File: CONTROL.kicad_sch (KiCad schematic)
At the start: 24 parts, among them J5 Conn_01x12-Socket, J6 Conn_01x12-Socket, J7 Conn_01x12-Header, J8 Conn_01x12-Header, M1 Fan_4pin, M2 Fan_4pin, U17 TMP1075, U30 T-Display-S3, U32 EMC2302-1, U33 TXU0102-DCU, U37 TMP1075, U38 TMP1075

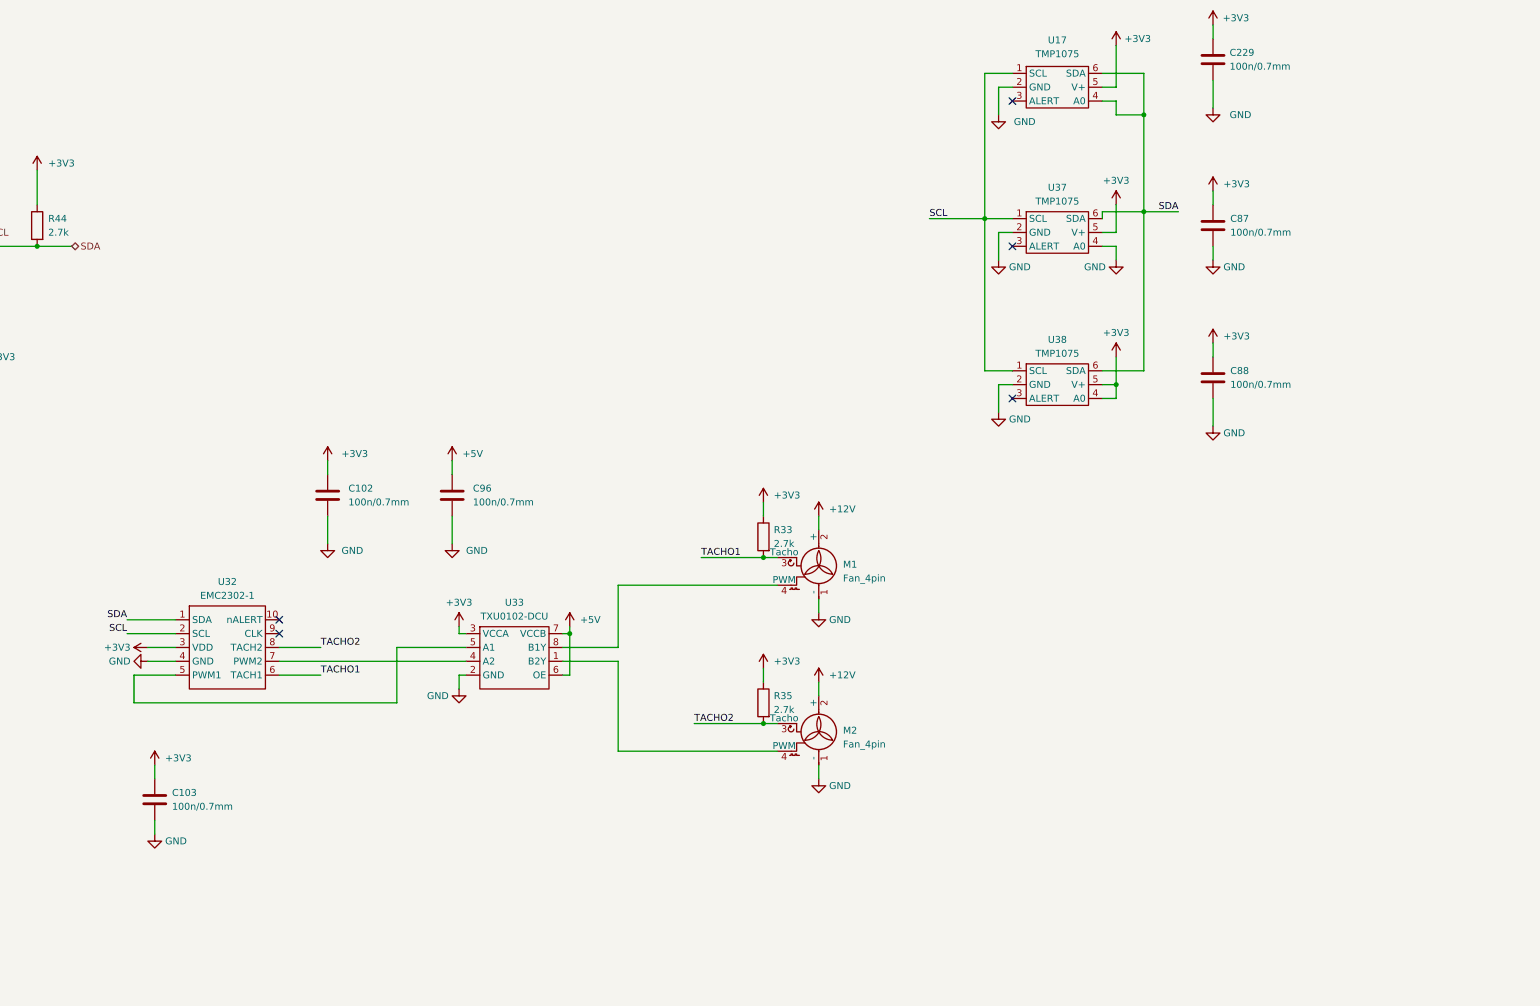
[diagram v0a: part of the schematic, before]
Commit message: shrinking layout to fit
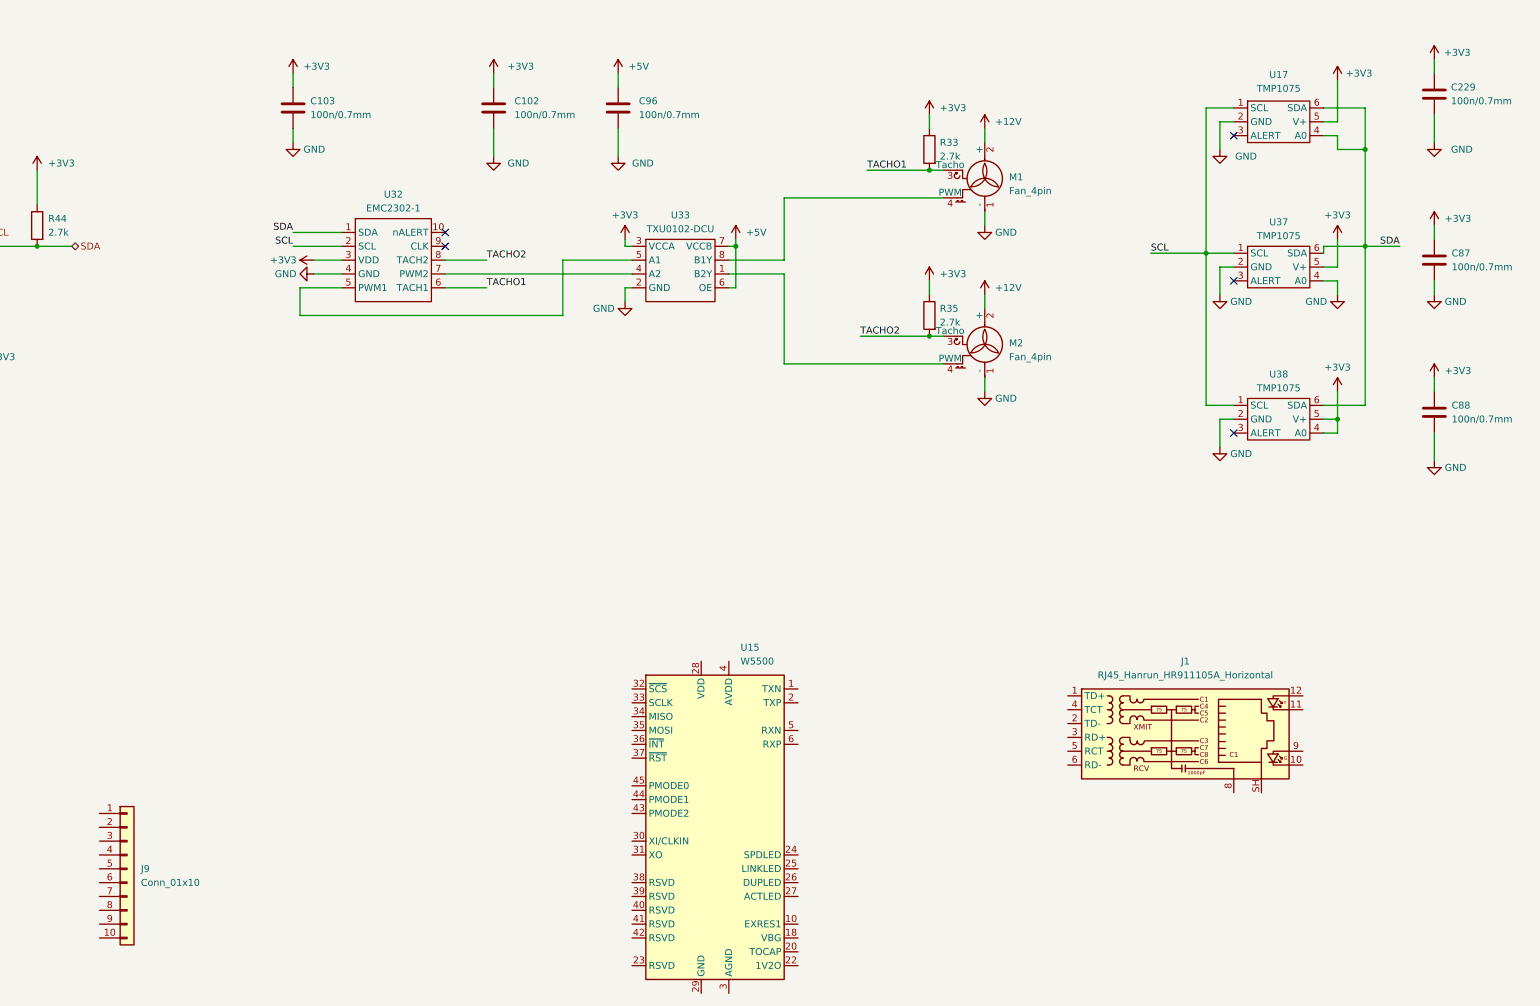
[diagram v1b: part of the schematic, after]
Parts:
- added J1: RJ45_Hanrun_HR911105A_Horizontal, Connector_RJ:RJ45_Hanrun_HR911105A_Horizontal, symbol Connector:RJ45_Hanrun_HR911105A_Horizontal
- added J9: Conn_01x10, Connector_PinHeader_2.54mm:PinHeader_1x10_P2.54mm_Vertical, symbol Connector_Generic:Conn_01x10
- added U15: W5500, Package_QFP:LQFP-48_7x7mm_P0.5mm, symbol Interface_Ethernet:W5500
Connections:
- new net: U15.11 (AVDD), U15.15 (AVDD), U15.17 (AVDD), U15.21 (AVDD), U15.4 (AVDD), U15.8 (AVDD)
- new net: U15.14 (AGND), U15.16 (AGND), U15.19 (AGND), U15.3 (AGND), U15.48 (AGND), U15.9 (AGND)
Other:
- moved on the sheet: C102, C103, C229, C87, C88, C96, M1, M2, R33, R35, U17, U32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

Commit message: W5500
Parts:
- removed J1: RJ45_Hanrun_HR911105A_Horizontal, Connector_RJ:RJ45_Hanrun_HR911105A_Horizontal, symbol Connector:RJ45_Hanrun_HR911105A_Horizontal
- removed U15: W5500, Package_QFP:LQFP-48_7x7mm_P0.5mm, symbol Interface_Ethernet:W5500
- added C128: 15pF, Capacitor_SMD:C_0603_1608Metric, symbol Parts:root_0_CAP_NOPOL_Parts.DbLib
- added C129: 15pF, CAP0402, symbol Parts:root_0_CAP_NOPOL_Parts.DbLib
- added C130, C131, C132, C134, C135, C136, C137, C138, C139: 100nF, CAP0402, symbol Parts:root_0_CAP_NOPOL_Parts.DbLib
- added C133: 4.7uF, CAP0603, symbol Parts:root_0_CAP_NOPOL_Parts.DbLib
- added C140, C141: 6.8nF, CAP0603, symbol Parts:root_1_CAP_NOPOL_Parts.DbLib
- added C142: 22n, CAP0603, symbol Parts:root_0_CAP_NOPOL_Parts.DbLib
- added C143: 1n, CAP1206, symbol Parts:root_1_CAP_NOPOL_Parts.DbLib
- added CON7: HR915340A, HR915340A, symbol Parts:root_0_HR915340A_Parts.DbLib
- added R112, R113, R114: 0R, RES0402, symbol Parts:root_2_Resistor_Parts.DbLib
- added R129, R52, R53: 4k7, RES0402, symbol Parts:root_1_Resistor_Parts.DbLib
- added R153: 33R, RES0402, symbol Parts:root_0_Resistor_Parts.DbLib
- added R41: 1M, Resistor_SMD:R_0603_1608Metric, symbol Parts:root_0_Resistor_Parts.DbLib
- added R42, R45, R46, R49: 3R3, RES0402, symbol Parts:root_0_Resistor_Parts.DbLib
- added R50, R54, R55, R56: 49R9, RES0402, symbol Parts:root_1_Resistor_Parts.DbLib
- added R51: 12k4, RES0402, symbol Parts:root_1_Resistor_Parts.DbLib
- added R57: 10R, RES0603, symbol Parts:root_1_Resistor_Parts.DbLib
- added R58, R59: 330R, RES0402, symbol Parts:root_1_Resistor_Parts.DbLib
- added R60: 1M, RES0603, symbol Parts:root_0_Resistor_Parts.DbLib
- added U12: W5500, QFP50P900X900X160-48N, symbol Parts:root_0_W5500_Parts.DbLib
- added X1: TXM25M0004322JBDDO00T, Crystal:Crystal_SMD_3225-4Pin_3.2x2.5mm, symbol Parts:root_3_XTAL_4_PINS_Parts.DbLib
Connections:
- net GND: now also C128.2, C129.2, C130.2, C131.2, C132.2, C133.2, C134.2, C135.2, C136.2, C137.2, C138.2, C139.2, C142.2, C143.1, R51.1, R60.1, U12.14 (AGND), U12.16 (AGND), U12.19 (AGND), U12.29 (GND), U12.3 (AGND), U12.48 (AGND), U12.9 (AGND), X1.2 (CASE), X1.4 (CASE)
- new net: R112.1, U12.45 (PMODE0)
- new net: R51.2, U12.10 (EXRES1)
- new net: CON7.11 (A), R59.1
- new net: C131.1, U12.22 (1V2O)
- new net: C139.1, CON7.5, R50.1, R54.1
- new net: C142.1, CON7.4, R57.1
- new net: CON7.9 (A), R58.1
- new net: R153.2, U12.34 (MISO)
- new net: C133.1, U12.20 (TOCAP)
- new net: R114.1, U12.43 (PMODE2)
- new net: R113.1, U12.44 (PMODE1)
- new net 3V3: R112.2, R113.2, R114.2, R129.2, R52.2, R53.2
- new net 3V3_ETH: C130.1, C132.1, C134.1, C135.1, C136.1, C137.1, C138.1, R55.2, R56.2, R57.2, R58.2, R59.2, U12.11 (AVDD), U12.15 (AVDD), U12.17 (AVDD), U12.21 (AVDD), U12.28 (VDD), U12.4 (AVDD), U12.8 (AVDD)
- new net ACT_LED_N: CON7.10 (C), U12.27 (ACTLED)
- new net ETHR_N: C141.1, R45.2, R50.2
- new net ETHR_P: C140.1, R49.2, R54.2
- new net ETH_RX_N: C141.2, CON7.6 (RD-)
- new net ETH_RX_P: C140.2, CON7.3 (RD+)
- new net ETH_R_N: R45.1, U12.5 (RXN)
- new net ETH_R_P: R49.1, U12.6 (RXP)
- new net ETH_TX_N: CON7.2 (TD-), R42.2, R56.1
- new net ETH_TX_P: CON7.1 (TD+), R46.2, R55.1
- new net ETH_T_N: R42.1, U12.1 (TXN)
- new net ETH_T_P: R46.1, U12.2 (TXP)
- new net FGND: C143.2, CON7.15 (Shield), CON7.16 (Shield), CON7.8 (CHS), R60.2
- new net LINK_LED_N: CON7.12 (C), U12.25 (LINKLED)
- new net W5500_CSN: R52.1, U12.32 (~{SCSN})
- new net W5500_INT_N: R53.1, U12.36 (~{INTN})
- new net W5500_MISO: R153.1
- new net W5500_MOSI: U12.35 (MOSI)
- new net W5500_RST_N: R129.1, U12.37 (~{RSTN})
- new net W5500_SCLK: U12.33 (SCLK)
- new net XI: C128.1, R41.1, U12.30 (XI), X1.1 (X1)
- new net XO: C129.1, R41.2, U12.31 (XO), X1.3 (X2)
- no-connect marks 10 -> 11
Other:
- note added: "check capacitance, 18pF??"
- moved on the sheet: J9

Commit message: 3v3 eth
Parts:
- removed CON7: HR915340A, HR915340A, symbol Parts:root_0_HR915340A_Parts.DbLib
- added C144, C145, C146, C147: 100nF, Capacitor_SMD:C_0603_1608Metric, symbol Parts:root_0_CAP_NOPOL_Parts.DbLib
- added C185, C189: 1u, Capacitor_SMD:C_0603_1608Metric, symbol Parts:root_0_CAP_NOPOL_Parts.DbLib
- added J1: RJ45_Hanrun_HR911105A_Horizontal, Connector_RJ:RJ45_Hanrun_HR911105A_Horizontal, symbol Connector:RJ45_Hanrun_HR911105A_Horizontal
- added L5: MH3261-601Y, Inductor_SMD:L_1206_3216Metric, symbol Parts:root_1_Inductor_Parts.DbLib
- C129, C130, C131, C132, C134, C135, C136, C137, C138, C139: footprint CAP0402 -> Capacitor_SMD:C_0603_1608Metric
- C133, C140, C141, C142: footprint CAP0603 -> Capacitor_SMD:C_0603_1608Metric
- C143: footprint CAP1206 -> Capacitor_SMD:C_1206_3216Metric
- R112, R113, R114, R129, R153, R42, R45, R46, R49, R50, R51, R52, R53, R54, R55, R56, R58, R59: footprint RES0402 -> Resistor_SMD:R_0603_1608Metric
- R57, R60: footprint RES0603 -> Resistor_SMD:R_0603_1608Metric
- U12: footprint QFP50P900X900X160-48N -> Package_QFP:LQFP-48_7x7mm_P0.5mm
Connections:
- net 3V3: now also C144.1, C145.1, C185.1, L5.1
- net 3V3_ETH: now also C146.1, C147.1, C189.1, L5.2
- net ACT_LED_N: now also J1.10
- net ETH_RX_N: now also J1.6 (RD-)
- net ETH_RX_P: now also J1.3 (RD+)
- net ETH_TX_N: now also J1.2 (TD-)
- net ETH_TX_P: now also J1.1 (TD+)
- net FGND: now also J1.8, J1.SH; no longer C143.2
- net GND: now also C144.2, C145.2, C146.2, C147.2, C185.2, C189.2
- net LINK_LED_N: now also J1.11
- net at R59.1: now also J1.9
- net at C139.1, R50.1, R54.1: now also J1.5 (RCT)
- net at C142.1, R57.1: now also J1.4 (TCT)
- net at R58.1: now also J1.12
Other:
- moved on the sheet: C143, R58, R59, R60

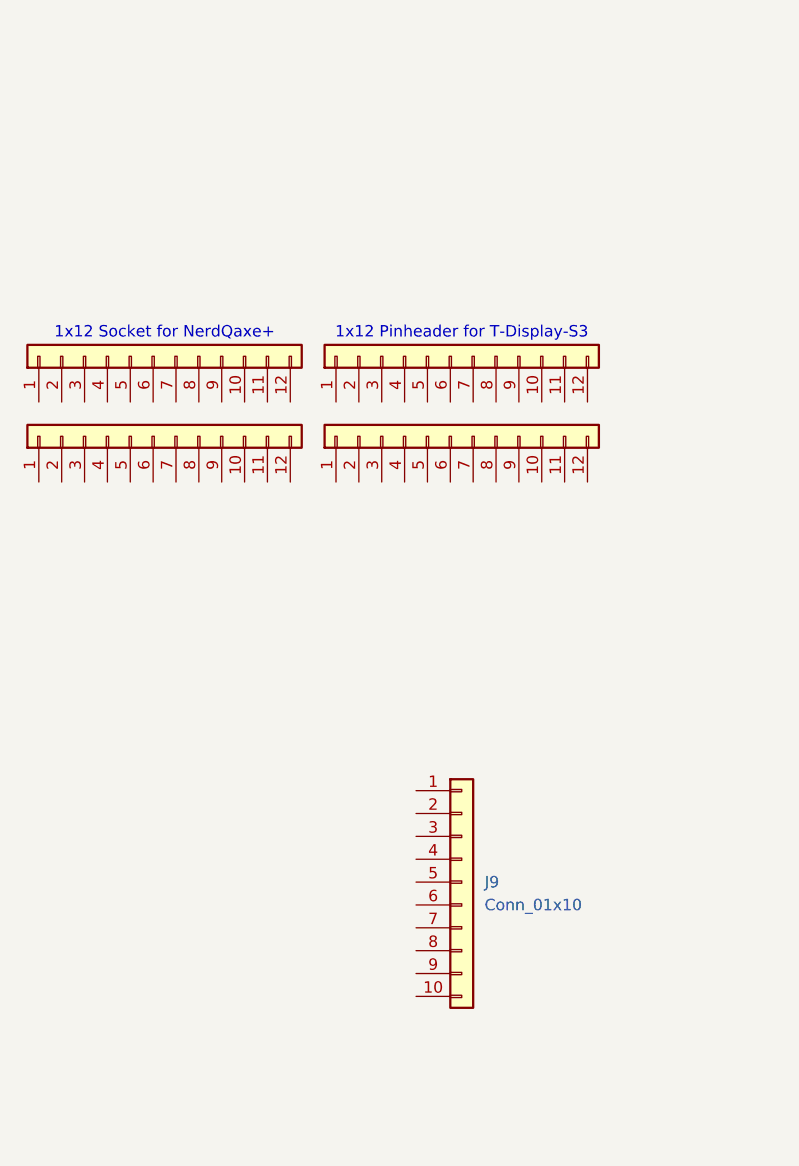
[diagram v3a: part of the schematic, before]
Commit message: placing W5500
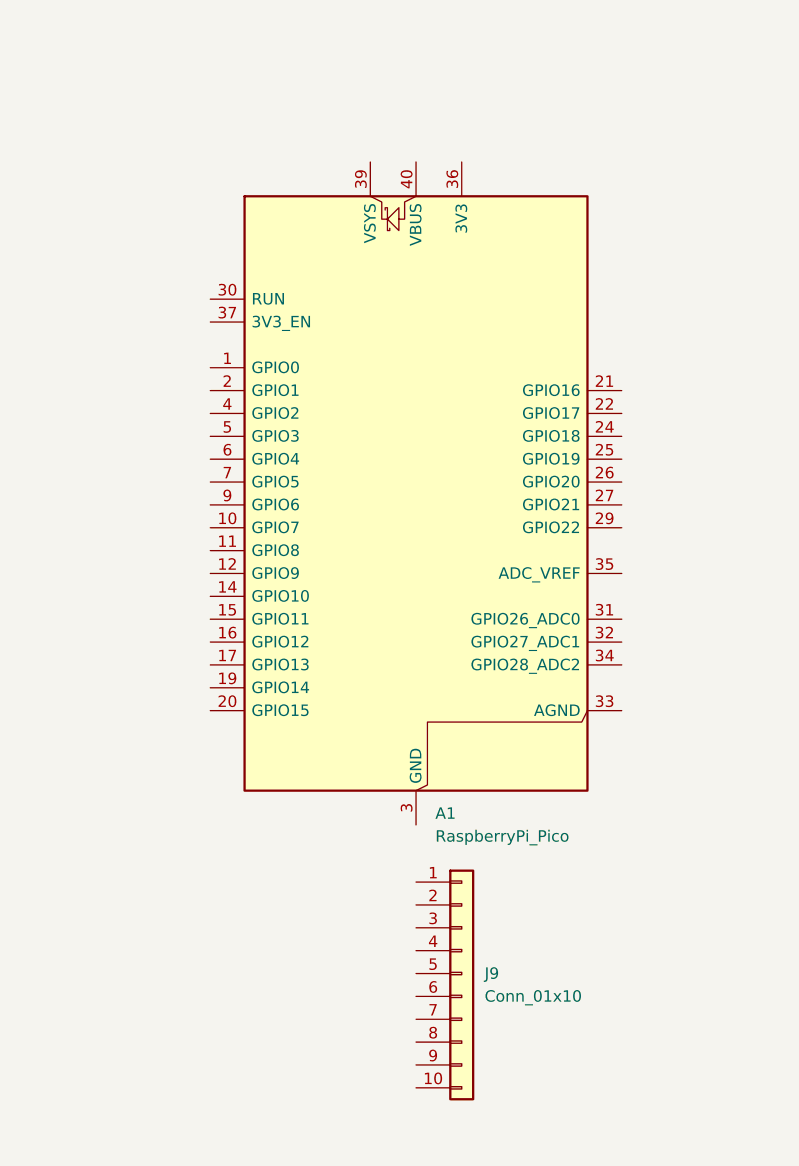
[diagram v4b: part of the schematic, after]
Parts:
- removed J5, J6: Conn_01x12-Socket, symbol Connector_Generic:Conn_01x12
- removed J7, J8: Conn_01x12-Header, symbol Connector_Generic:Conn_01x12
- added A1: RaspberryPi_Pico, Module:RaspberryPi_Pico_Common_Unspecified, symbol MCU_Module:RaspberryPi_Pico
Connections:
- new net: A1.13 (GND), A1.18 (GND), A1.23 (GND), A1.28 (GND), A1.3 (GND), A1.38 (GND), A1.8 (GND)
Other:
- note removed: "1x12 Pinheader for T-Display-S3"
- note removed: "1x12 Socket for NerdQaxe+"
- moved on the sheet: J9

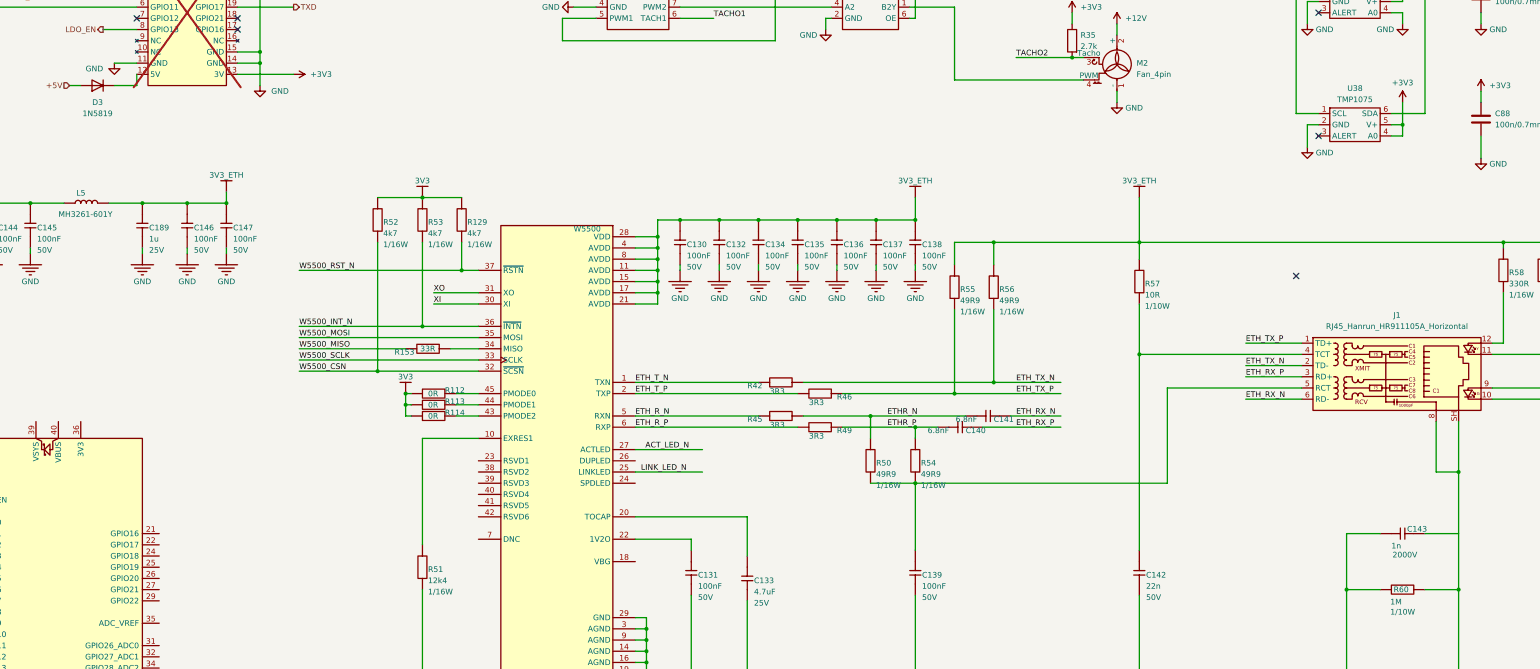
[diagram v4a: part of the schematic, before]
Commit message: w5500 placed
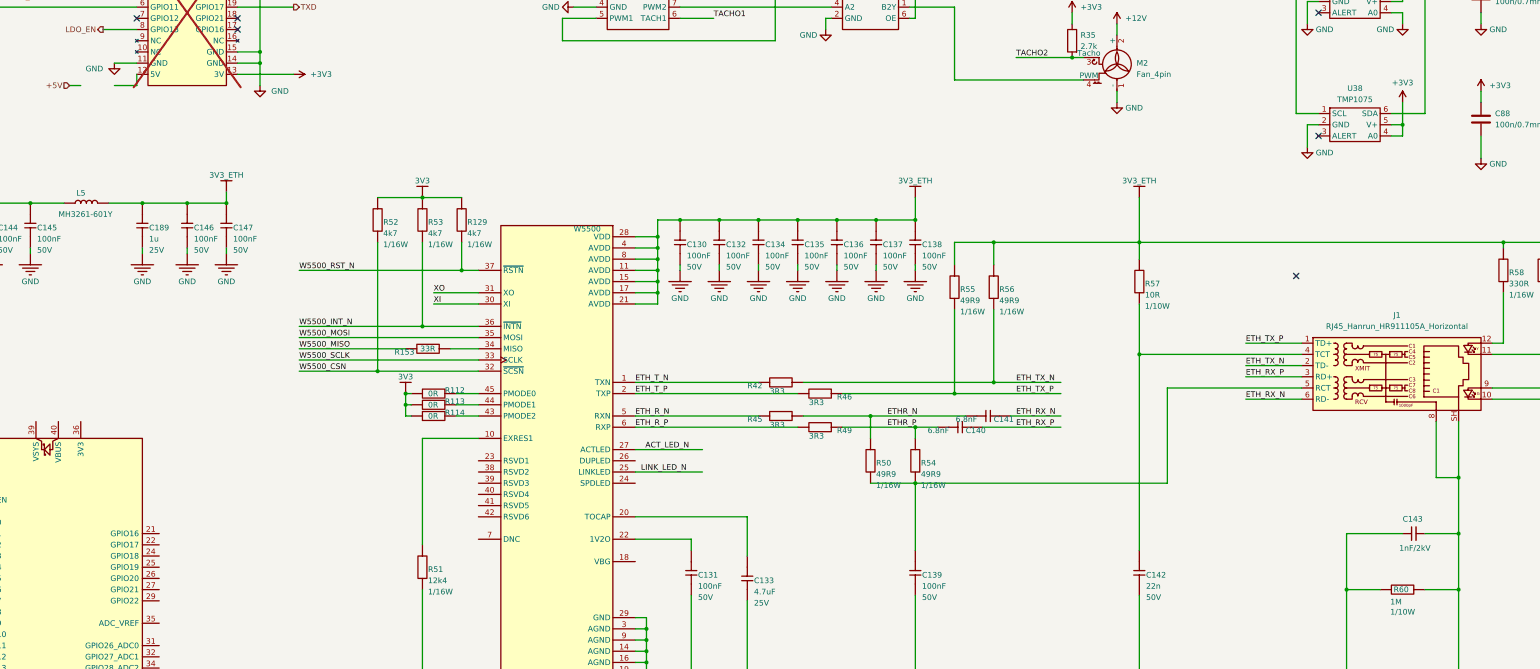
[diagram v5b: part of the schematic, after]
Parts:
- removed C143: 1n, Capacitor_SMD:C_1206_3216Metric, symbol Parts:root_1_CAP_NOPOL_Parts.DbLib
- removed D3: 1N5819, Diode_SMD:D_SOD-123, symbol Diode:US1D
- added C143: 1nF/2kV, Capacitor_SMD:C_1206_3216Metric, symbol Device:C_Small
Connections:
- net FGND: now also C143.2
- net GND: now also C143.1
